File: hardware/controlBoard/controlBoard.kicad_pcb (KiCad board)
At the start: 2 copper layers, 55 x 55 mm, 36 parts, among them J1 Conn_01x10_Pin, J2 USB_C_Receptacle_USB2.0_14P, T1 BC847, T2 BC847, U2 LM1117DT-3.3, U3 CH340G, U4 DS3231M, U5 ESP32-WROOM-32D, Y2 405I35D25M00000

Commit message: Finalize PCB design
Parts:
- Y2: value 405I35D25M00000 -> 12MHz

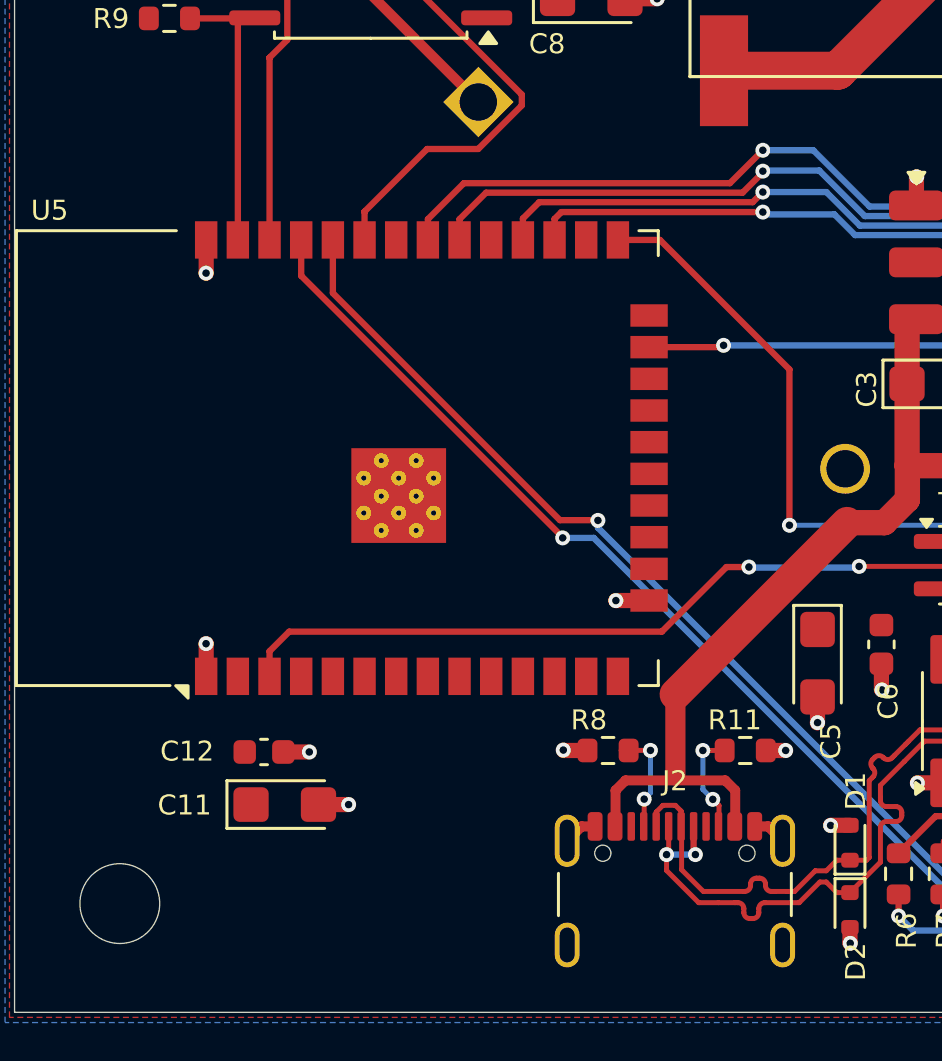
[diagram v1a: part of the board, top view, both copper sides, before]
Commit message: Fix auto-programming circuit issue
- Add pullups to EN and IO0 pins.
- Add 100nF ceramic capacitor between EN and GND to improve timimng.
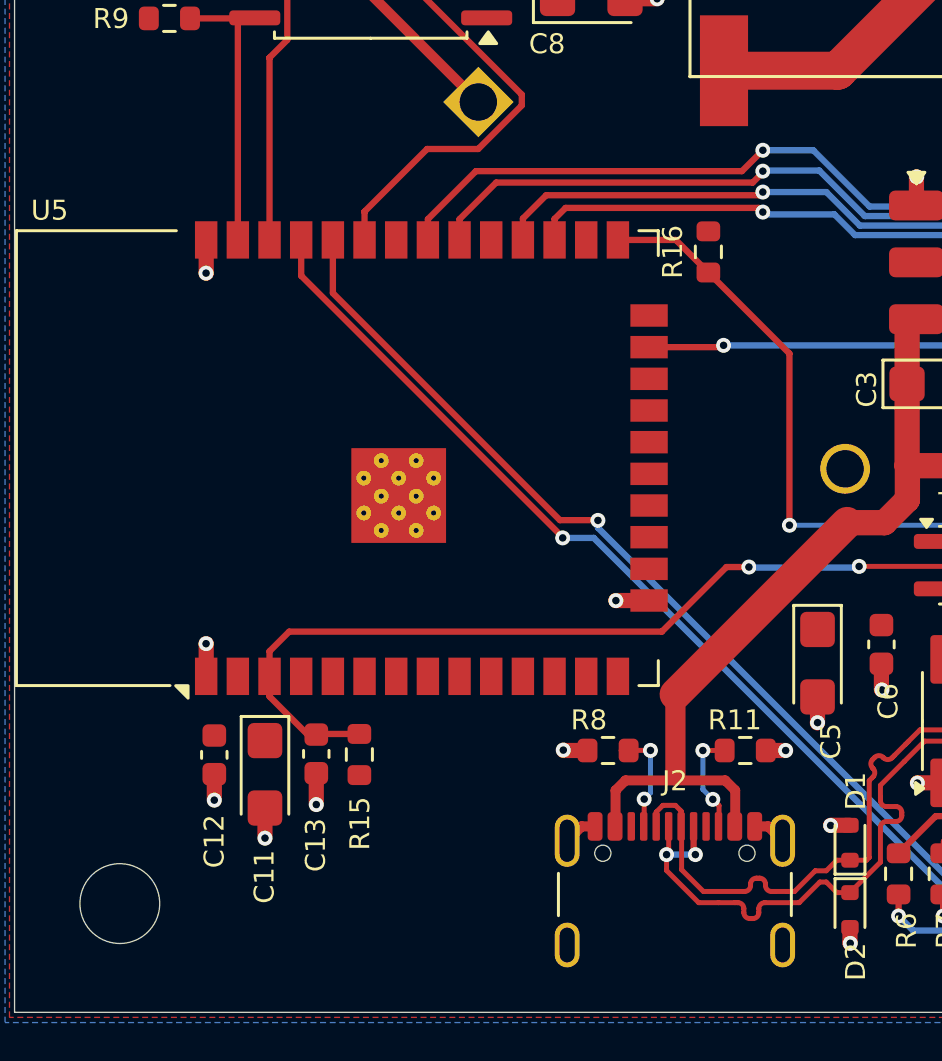
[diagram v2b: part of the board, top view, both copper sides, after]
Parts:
- added C13: 100n, Capacitor_SMD:C_0603_1608Metric, F.Cu at (133.1, 122.1)
- added R15: 12k, Resistor_SMD:R_0603_1608Metric, F.Cu at (134.8, 122.2)
- added R16: 12k, Resistor_SMD:R_0603_1608Metric, F.Cu at (148.8, 102.0)
- moved C12 2.00 mm to (129.0, 122.2), turned to -90 degrees
- moved C11 1.45 mm to (131.0, 123.0), turned to -90 degrees
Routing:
- net /EN: track 30.9 -> 35.9 mm
- net GND: track 22.9 -> 24.1 mm, vias 55 -> 56
